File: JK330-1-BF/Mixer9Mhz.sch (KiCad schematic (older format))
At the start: 12 parts

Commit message: MAJ  composants
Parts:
- C1, C2: value CP -> 10U
- D1, D2: value DIODE -> MA4P1250
- RVAR1: value RVAR -> 100
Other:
- note added: "Multitour"
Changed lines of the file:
@@
-EESchema Schematic File Version 2  date 2013-03-25 22:18:17
+EESchema Schematic File Version 2  date 29/04/2013 22:12:34
 LIBS:power
 LIBS:CEN-SCHEMA
@@
 Sheet 2 6
 Title ""
-Date "25 mar 2013"
+Date "29 apr 2013"
 Rev ""
 Comp ""
@@
 P 5025 2600
 F 0 "C1" H 5075 2700 50  0000 L CNN
-F 1 "CP" H 5075 2500 50  0000 L CNN
+F 1 "10U" H 5075 2500 50  0000 L CNN
 F 2 "" H 5025 2600 60  0001 C CNN
 F 3 "" H 5025 2600 60  0001 C CNN
@@
 U 1 1 514E2FF7
 P 4525 3000
-F 0 "C2" H 4575 3100 50  0000 L CNN
-F 1 "CP" H 4575 2900 50  0000 L CNN
+F 0 "C2" V 4625 3075 50  0000 L CNN
+F 1 "10U" V 4625 2825 50  0000 L CNN
 F 2 "" H 4525 3000 60  0001 C CNN
 F 3 "" H 4525 3000 60  0001 C CNN
@@
 U 1 1 514E2DD7
 P 5175 3350
-F 0 "RVAR1" V 5125 3450 50  0000 C CNN
-F 1 "RVAR" V 5225 3450 50  0000 C CNN
+F 0 "RVAR1" V 5125 3075 50  0000 C CNN
+F 1 "100" V 5125 3425 50  0000 C CNN
 F 2 "" H 5175 3350 60  0001 C CNN
 F 3 "" H 5175 3350 60  0001 C CNN
@@
 U 1 1 514E2D7C
 P 6150 4700
-F 0 "R3" V 6100 4800 50  0000 C CNN
-F 1 "1k" V 6200 4800 50  0000 C CNN
+F 0 "R3" H 6050 4700 50  0000 C CNN
+F 1 "1k" H 6050 4600 50  0000 C CNN
 F 2 "" H 6150 4700 60  0001 C CNN
 F 3 "" H 6150 4700 60  0001 C CNN
@@
 U 1 1 514E2D6E
 P 6150 2750
-F 0 "R1" V 6100 2850 50  0000 C CNN
-F 1 "1k" V 6200 2850 50  0000 C CNN
+F 0 "R1" H 6050 2700 50  0000 C CNN
+F 1 "1k" H 6050 2600 50  0000 C CNN
 F 2 "" H 6150 2750 60  0001 C CNN
 F 3 "" H 6150 2750 60  0001 C CNN
@@
 U 1 1 514E2D5C
 P 5750 3800
-F 0 "C4" H 5800 3900 50  0000 L CNN
-F 1 "1n" H 5800 3700 50  0000 L CNN
+F 0 "C4" V 5800 3900 50  0000 L CNN
+F 1 "1n" V 5800 3650 50  0000 L CNN
 F 2 "" H 5750 3800 60  0001 C CNN
 F 3 "" H 5750 3800 60  0001 C CNN
@@
 U 1 1 514E2D51
 P 5500 3500
-F 0 "MX1" H 5500 3500 60  0000 C CNN
-F 1 "SBL-1" H 5500 3500 60  0000 C CNN
+F 0 "MX1" H 6300 3350 60  0000 C CNN
+F 1 "SBL-1" H 6350 3050 60  0000 C CNN
 F 2 "" H 5500 3500 60  0001 C CNN
 F 3 "" H 5500 3500 60  0001 C CNN
@@
 U 1 1 514E29B3
 P 6400 3800
-F 0 "R2" V 6350 3900 50  0000 C CNN
-F 1 "1k" V 6450 3900 50  0000 C CNN
+F 0 "R2" V 6450 3750 50  0000 C CNN
+F 1 "1k" V 6450 3600 50  0000 C CNN
 F 2 "" H 6400 3800 60  0001 C CNN
 F 3 "" H 6400 3800 60  0001 C CNN
@@
 U 1 1 514E299B
 P 6500 4500
-F 0 "C5" H 6550 4600 50  0000 L CNN
-F 1 "1n" H 6550 4400 50  0000 L CNN
+F 0 "C5" V 6550 4600 50  0000 L CNN
+F 1 "1n" V 6550 4350 50  0000 L CNN
 F 2 "" H 6500 4500 60  0001 C CNN
 F 3 "" H 6500 4500 60  0001 C CNN
@@
 U 1 1 514E2995
 P 6500 3150
-F 0 "C3" H 6550 3250 50  0000 L CNN
-F 1 "1n" H 6550 3050 50  0000 L CNN
+F 0 "C3" V 6550 3250 50  0000 L CNN
+F 1 "1n" V 6550 3000 50  0000 L CNN
 F 2 "" H 6500 3150 60  0001 C CNN
 F 3 "" H 6500 3150 60  0001 C CNN
@@
 U 1 1 514E2901
 P 6150 3400
-F 0 "D1" H 6150 3500 40  0000 C CNN
-F 1 "DIODE" H 6150 3300 40  0000 C CNN
+F 0 "D1" V 6100 3300 40  0000 C CNN
+F 1 "MA4P1250" V 6250 3200 40  0000 C CNN
 F 2 "" H 6150 3400 60  0001 C CNN
 F 3 "" H 6150 3400 60  0001 C CNN
@@
 U 1 1 514E28F2
 P 6150 4200
-F 0 "D2" H 6150 4300 40  0000 C CNN
-F 1 "DIODE" H 6150 4100 40  0000 C CNN
+F 0 "D2" V 6200 4300 40  0000 C CNN
+F 1 "MA4P1250" V 6050 4400 40  0000 C CNN
 F 2 "" H 6150 4200 60  0001 C CNN
 F 3 "" H 6150 4200 60  0001 C CNN
@@
 	0    -1   -1   0
 $EndComp
+Text Notes 4900 3500 0    60   ~ 0
+Multitour
 $EndSCHEMATC

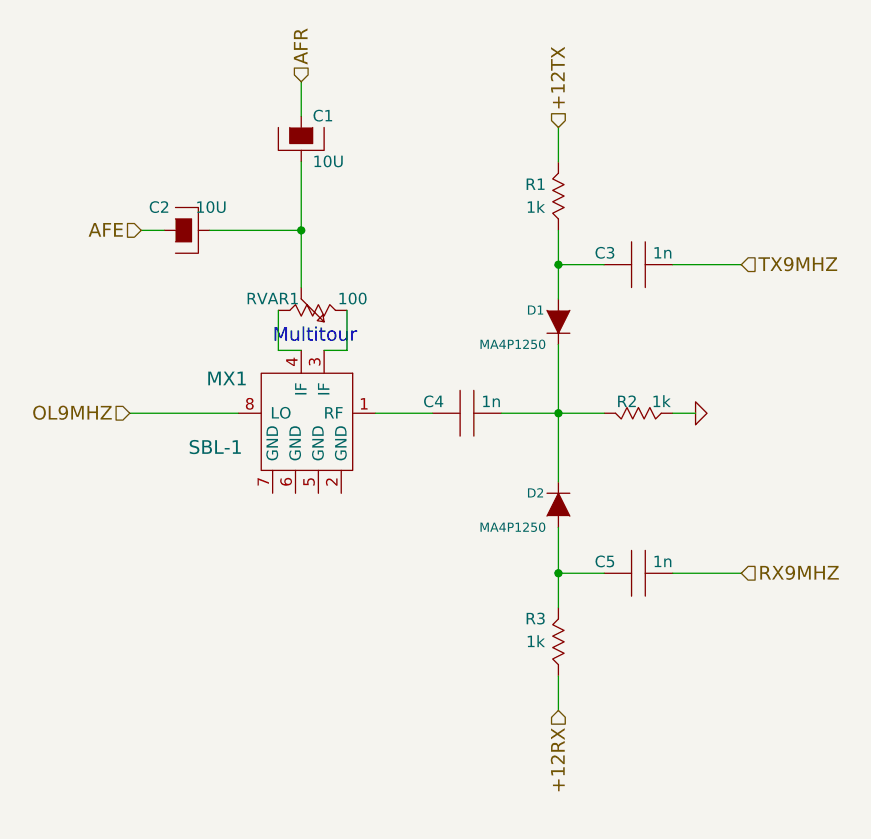
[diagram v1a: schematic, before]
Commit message: Rajout commande PTT
+12VTV
+12VRX
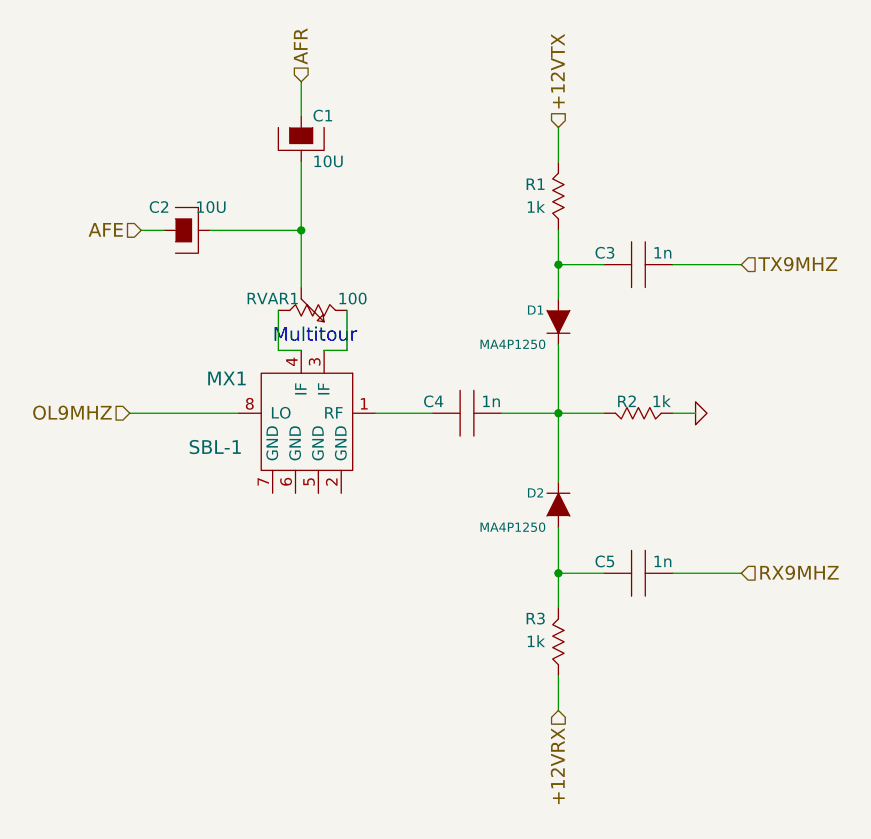
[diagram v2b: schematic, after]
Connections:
- net +12RX renamed +12VRX
- net +12TX renamed +12VTX
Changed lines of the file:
@@
-EESchema Schematic File Version 2  date 29/04/2013 22:12:34
+EESchema Schematic File Version 2  date 30/04/2013 22:23:42
 LIBS:power
 LIBS:CEN-SCHEMA
@@
 Sheet 2 6
 Title ""
-Date "29 apr 2013"
+Date "30 apr 2013"
 Rev ""
 Comp ""
@@
 $EndComp
 Text HLabel 6150 5100 3    60   Input ~ 0
-+12RX
++12VRX
 Text HLabel 6150 2550 1    60   Input ~ 0
-+12TX
++12VTX
 $Comp
 L RVAR RVAR1

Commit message: MAJ mineur
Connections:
- net GND: now also MX1.2 (GND), MX1.5 (GND), MX1.6 (GND), MX1.7 (GND)
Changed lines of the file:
@@
-EESchema Schematic File Version 2  date 20/05/2013 22:53:16
+EESchema Schematic File Version 2  date 04/06/2013 21:43:31
 LIBS:power
 LIBS:CEN-SCHEMA
@@
 Sheet 2 6
 Title ""
-Date "20 may 2013"
+Date "4 jun 2013"
 Rev ""
 Comp ""
@@
 Text Notes 4900 3500 0    60   ~ 0
 Multitour
+Wire Wire Line
+	4900 4150 4900 4200
+Wire Wire Line
+	4900 4200 5200 4200
+Wire Wire Line
+	5200 4200 5200 4150
+Wire Wire Line
+	5000 4150 5000 4300
+Connection ~ 5000 4200
+Wire Wire Line
+	5100 4150 5100 4200
+Connection ~ 5100 4200
+$Comp
+L GND #PWR?
+U 1 1 51AE4B7A
+P 5000 4300
+F 0 "#PWR?" H 5000 4300 30  0001 C CNN
+F 1 "GND" H 5000 4230 30  0001 C CNN
+F 2 "" H 5000 4300 60  0000 C CNN
+F 3 "" H 5000 4300 60  0000 C CNN
+	1    5000 4300
+	1    0    0    -1
+$EndComp
 $EndSCHEMATC
